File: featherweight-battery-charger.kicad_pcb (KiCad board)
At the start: 2 copper layers, 16 parts, among them J1 G125-MH104M4-04AD000P, J2 Conn_01x02, U1 MCP73832-2-OT, U2 TPS561208DDCR

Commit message: Started Layout and Routing
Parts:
- F1, R1: moved to B.Cu
- L1: value ASPI-4030S-4R7M-T (4.7uH) -> NRS4018T4R7MDGJ (4.7uH); footprint Inductor_SMD:L_Abracon_ASPI-4030S -> Inductor_SMD:L_Taiyo-Yuden_NR-40xx_HandSoldering
- moved J2 62.3 mm to (125.0, 119.6)
- moved U1 61.8 mm to (114.8, 121.3)
- moved C1 61.0 mm to (126.3, 116.3)
- moved R1 58.1 mm to (113.6, 120.3), turned to 180 degrees
- moved R2 55.9 mm to (111.8, 119.1), turned to -90 degrees
- moved D1 53.0 mm to (114.8, 118.3)
- moved L1 31.1 mm to (141.5, 67.7), turned to -90 degrees
- moved U2 27.7 mm to (146.6, 63.9), turned to 90 degrees
- moved R3 25.0 mm to (148.1, 59.8), turned to 90 degrees
- moved R4 24.0 mm to (147.2, 59.8), turned to -90 degrees
- moved C2 23.6 mm to (144.3, 63.2), turned to -90 degrees
- moved C3 20.3 mm to (146.6, 68.3), turned to 180 degrees
- moved C4 19.9 mm to (146.7, 69.2)
- moved C5 17.0 mm to (144.6, 68.3), turned to 180 degrees
- moved F1 12.8 mm to (149.5, 65.8), turned to 180 degrees
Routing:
- net GND: track 0.00 -> 5.30 mm
- net +12V: track 0.00 -> 4.77 mm
- net +5V: track 0.00 -> 3.24 mm
- net Net-(U2-VFB): track 0.00 -> 2.81 mm
- net Net-(U2-SW): track 13.8 -> 11.5 mm
- net /STAT: track 0.00 -> 2.25 mm
- net Net-(J1-+12V): track 0.00 -> 1.89 mm
- net Net-(D1-K): track 0.00 -> 1.75 mm

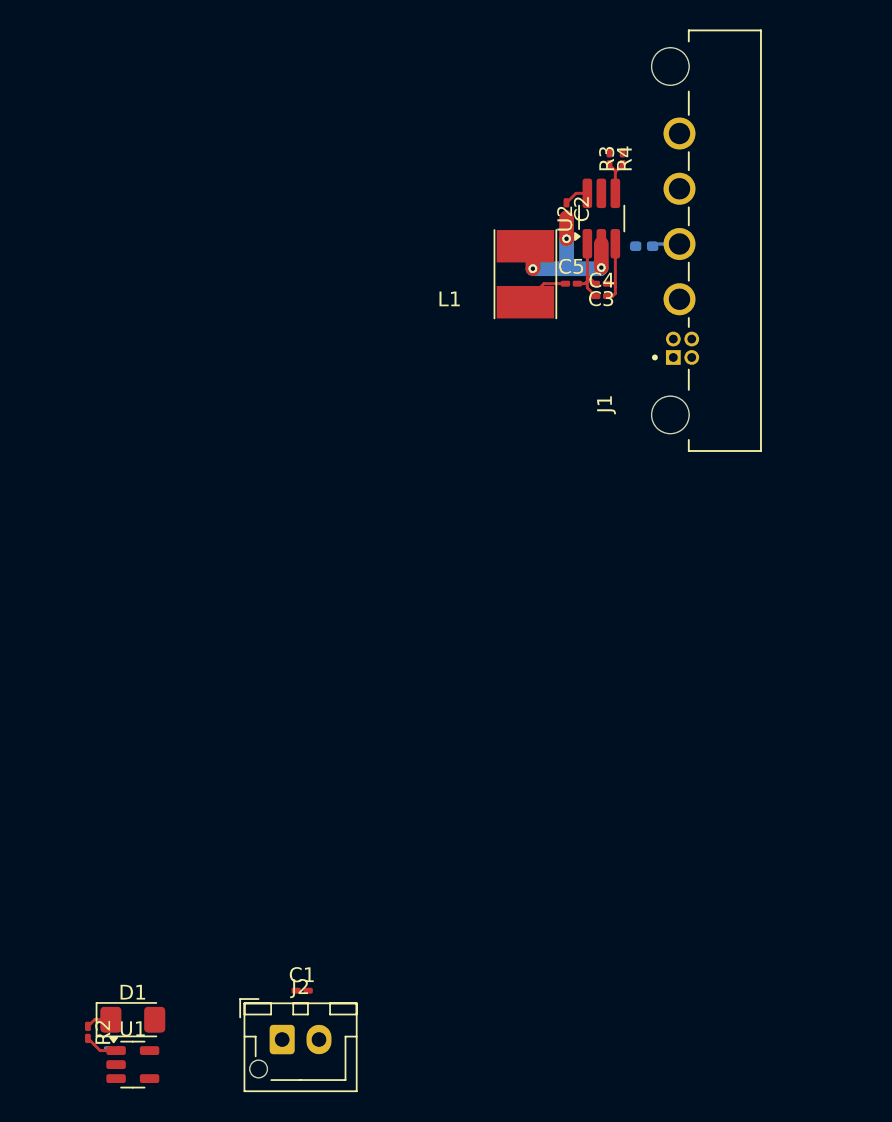
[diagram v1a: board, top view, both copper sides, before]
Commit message: Did most of the layout and routing, need to finish silkscreen and then check everything
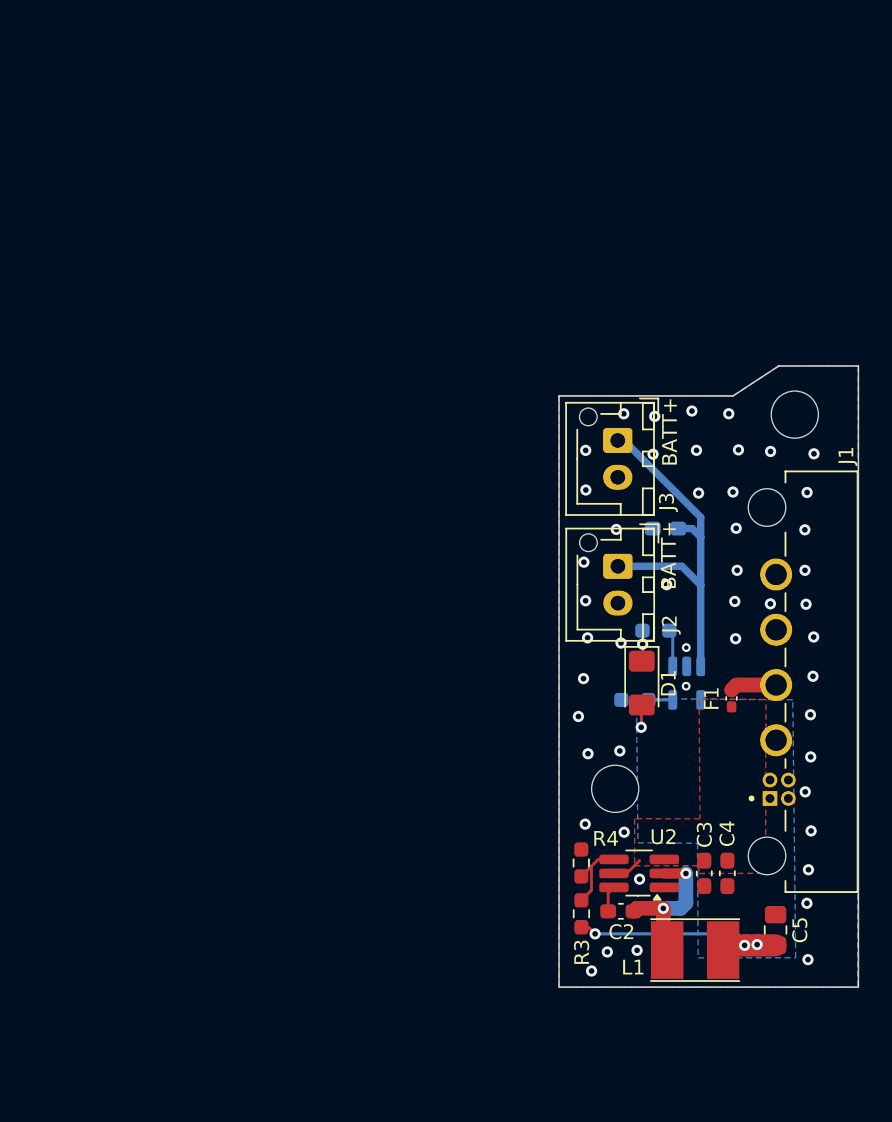
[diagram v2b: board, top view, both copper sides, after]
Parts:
- added H1: MountingHole, MountingHole:MountingHole_3.2mm_M3, F.Cu at (159.8, 77.2)
- added H2: MountingHole, MountingHole:MountingHole_3.2mm_M3, F.Cu at (147.6, 102.6)
- added J3: Conn_01x02, Connector_JST:JST_XH_B2B-XH-AM_1x02_P2.50mm_Vertical, F.Cu at (147.8, 79.0)
- C1: footprint Capacitor_SMD:C_0201_0603Metric_Pad0.64x0.40mm_HandSolder -> Capacitor_SMD:C_0603_1608Metric_Pad1.08x0.95mm_HandSolder; moved to B.Cu
- C2: footprint Capacitor_SMD:C_0201_0603Metric_Pad0.64x0.40mm_HandSolder -> Capacitor_SMD:C_0603_1608Metric_Pad1.08x0.95mm_HandSolder
- C3, C4: value 10uF -> CL10A106MA8NRNC (10uF); footprint Capacitor_SMD:C_0201_0603Metric_Pad0.64x0.40mm_HandSolder -> Capacitor_SMD:C_0603_1608Metric_Pad1.08x0.95mm_HandSolder
- C5: value 47uF -> GRM21BR61A476ME15L (47uF); footprint Capacitor_SMD:C_0201_0603Metric_Pad0.64x0.40mm_HandSolder -> Capacitor_SMD:C_0805_2012Metric_Pad1.18x1.45mm_HandSolder
- F1: moved to F.Cu
- R1, R3, R4: footprint Resistor_SMD:R_0201_0603Metric_Pad0.64x0.40mm_HandSolder -> Resistor_SMD:R_0603_1608Metric_Pad0.98x0.95mm_HandSolder
- R2: footprint Resistor_SMD:R_0201_0603Metric_Pad0.64x0.40mm_HandSolder -> Resistor_SMD:R_0603_1608Metric_Pad0.98x0.95mm_HandSolder; moved to B.Cu
- U1: moved to B.Cu
- moved R3 51.3 mm to (145.3, 111.1), turned to -90 degrees
- moved R4 47.8 mm to (145.3, 107.7)
- moved C2 47.8 mm to (148.0, 110.9), turned to 0 degrees
- moved L1 47.3 mm to (153.0, 113.6), turned to 0 degrees
- moved R2 47.2 mm to (150.3, 91.9), turned to 0 degrees
- moved C5 46.0 mm to (158.5, 112.2), turned to -90 degrees
- moved U1 45.7 mm to (152.4, 95.4), turned to -90 degrees
- moved U2 44.5 mm to (149.2, 108.4), turned to 180 degrees
- moved R1 42.5 mm to (148.9, 96.6)
- moved D1 41.4 mm to (149.4, 95.4), turned to -90 degrees
- moved C3 40.6 mm to (153.6, 108.4), turned to -90 degrees
- moved C4 40.1 mm to (155.2, 108.4), turned to 90 degrees
- moved C1 39.9 mm to (151.0, 85.0), turned to 180 degrees
- moved J2 39.4 mm to (147.8, 87.5), turned to -90 degrees
- moved F1 31.3 mm to (155.5, 96.5), turned to -90 degrees
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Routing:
- net Net-(J2-Pin_1): track 0.00 -> 25.8 mm
- net +5V: track 3.24 -> 16.3 mm, vias 0 -> 4
- net GND: track 5.30 -> 0.00 mm, vias 0 -> 49
- net +12V: track 4.77 -> 1.25 mm
- net Net-(U2-VFB): track 2.81 -> 5.28 mm
- net Net-(U2-SW): track 11.5 -> 9.84 mm, vias 3 -> 2
- net Net-(U1-PROG): track 0.00 -> 1.46 mm
- net Net-(J1-+12V): track 1.89 -> 3.17 mm
- net Net-(D1-K): track 1.75 -> 2.03 mm, vias 0 -> 1
- added copper zone on F.Cu, net +12V
- added copper zone on B.Cu, net +5V
- added copper zone on B.Cu, net GND
- added copper zone on F.Cu, net GND
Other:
- board outline added: 20.3 x 42.2 mm
- board text added: "BATT+"

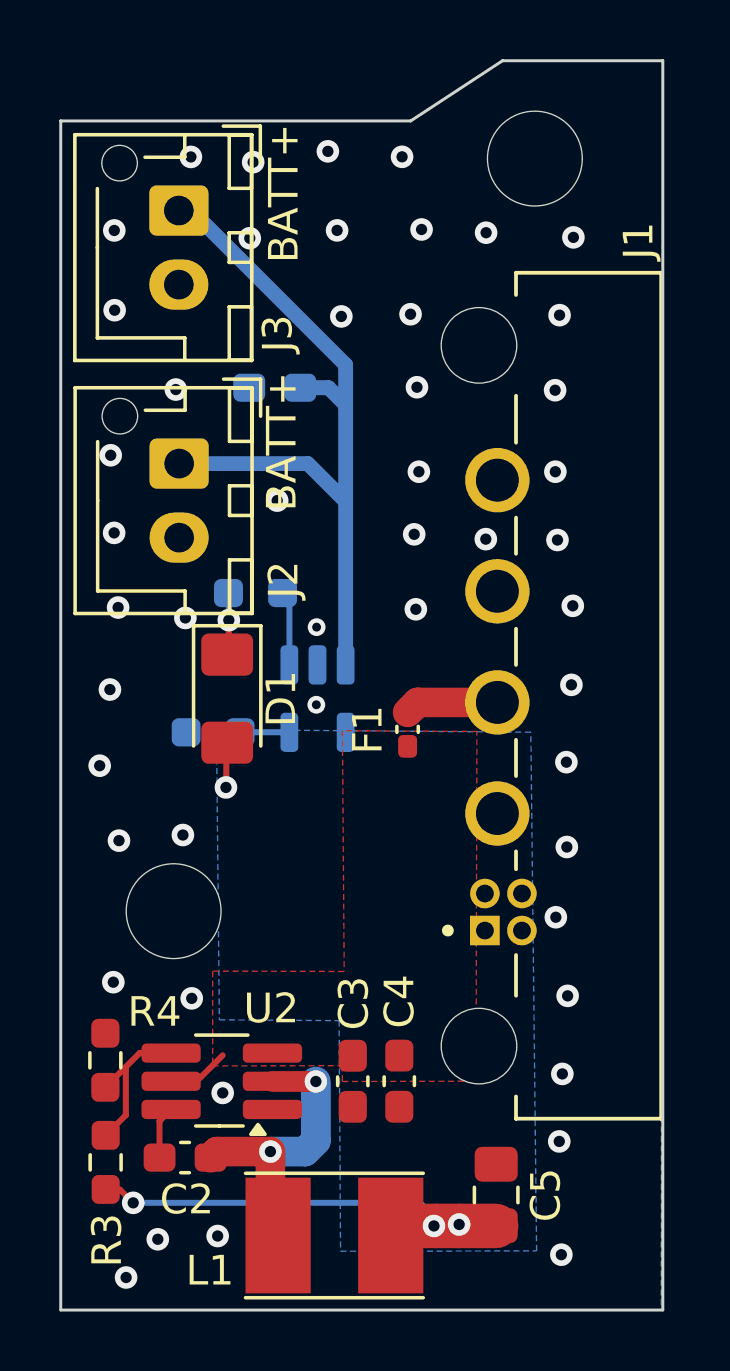
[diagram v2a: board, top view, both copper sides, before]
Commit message: Fixed some routing and silkscreen, should be done hopefully
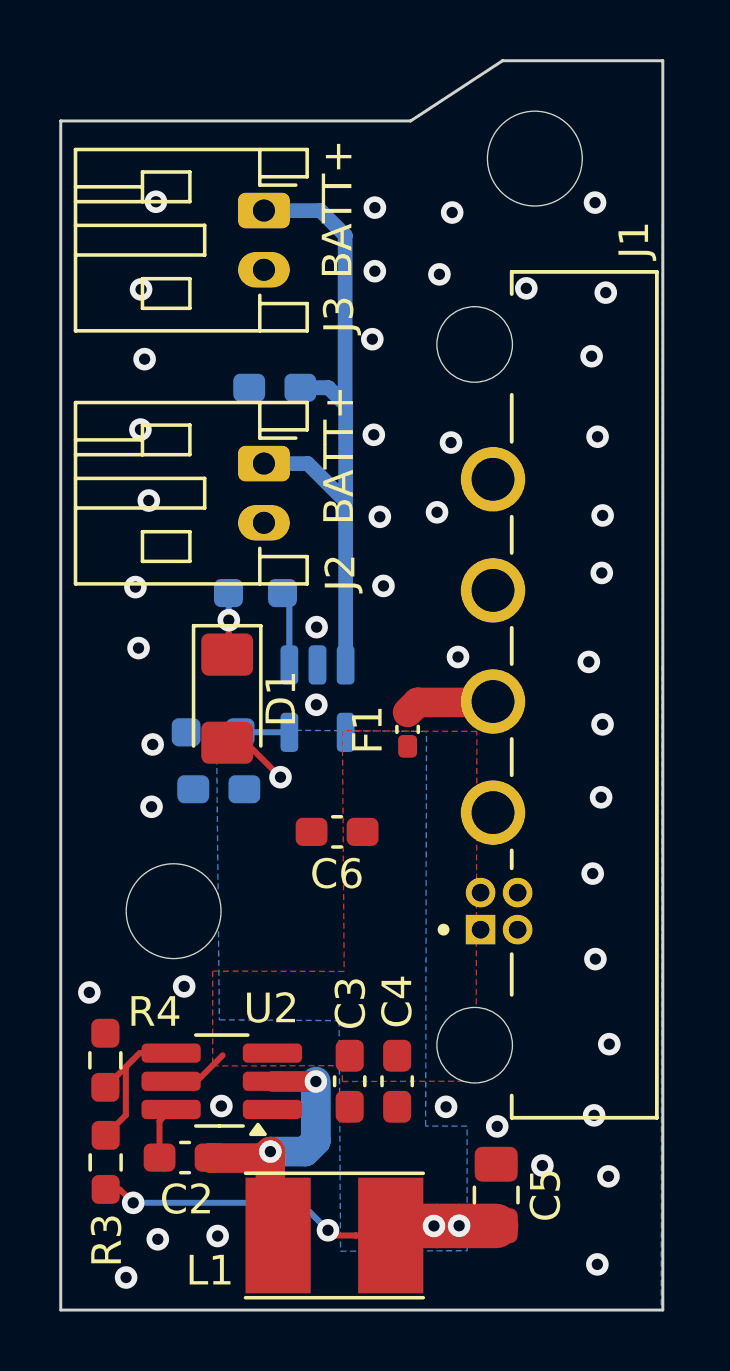
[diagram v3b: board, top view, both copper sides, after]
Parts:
- added C6: 0.1uF, Capacitor_SMD:C_0603_1608Metric_Pad1.08x0.95mm_HandSolder, F.Cu at (153.1, 99.9)
- added C7: 0.1uF, Capacitor_SMD:C_0603_1608Metric_Pad1.08x0.95mm_HandSolder, B.Cu at (149.1, 98.5)
- F1: value ERB-RD0R50X -> ERB-RD0R50X (500mA)
- J2, J3: footprint Connector_JST:JST_XH_B2B-XH-AM_1x02_P2.50mm_Vertical -> Connector_JST:JST_PH_S2B-PH-K_1x02_P2.00mm_Horizontal
- moved J3 2.87 mm to (150.6, 79.0)
- moved J2 2.86 mm to (150.6, 87.5)
- moved J1 0.15 mm to (161.4, 95.3)
- moved C3 0.10 mm to (153.5, 108.4)
- moved C4 0.07 mm to (155.1, 108.4)
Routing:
- net Net-(J2-Pin_1): track 25.8 -> 22.7 mm
- net +5V: track 16.3 -> 15.1 mm, vias 4 -> 5
- net GND: vias 49 -> 47

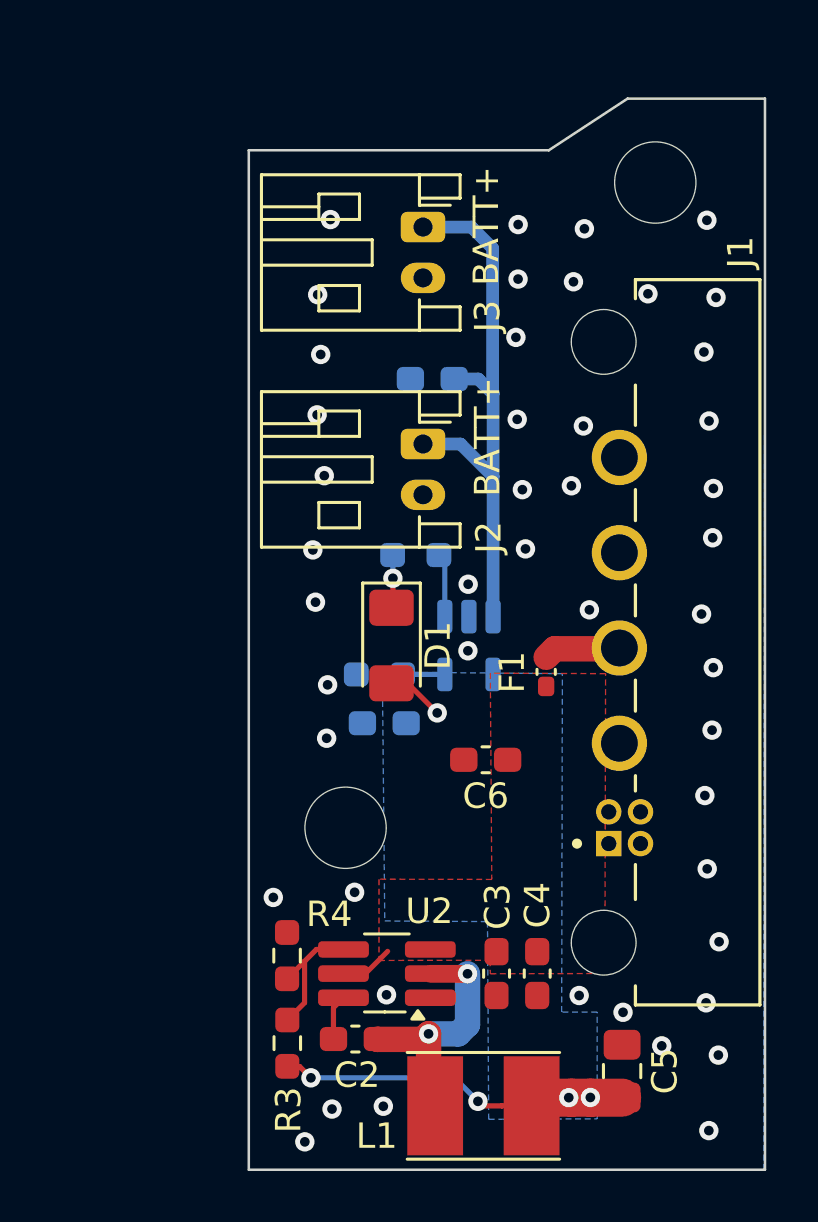
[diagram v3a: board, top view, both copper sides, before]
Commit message: Changed Layout and Routing
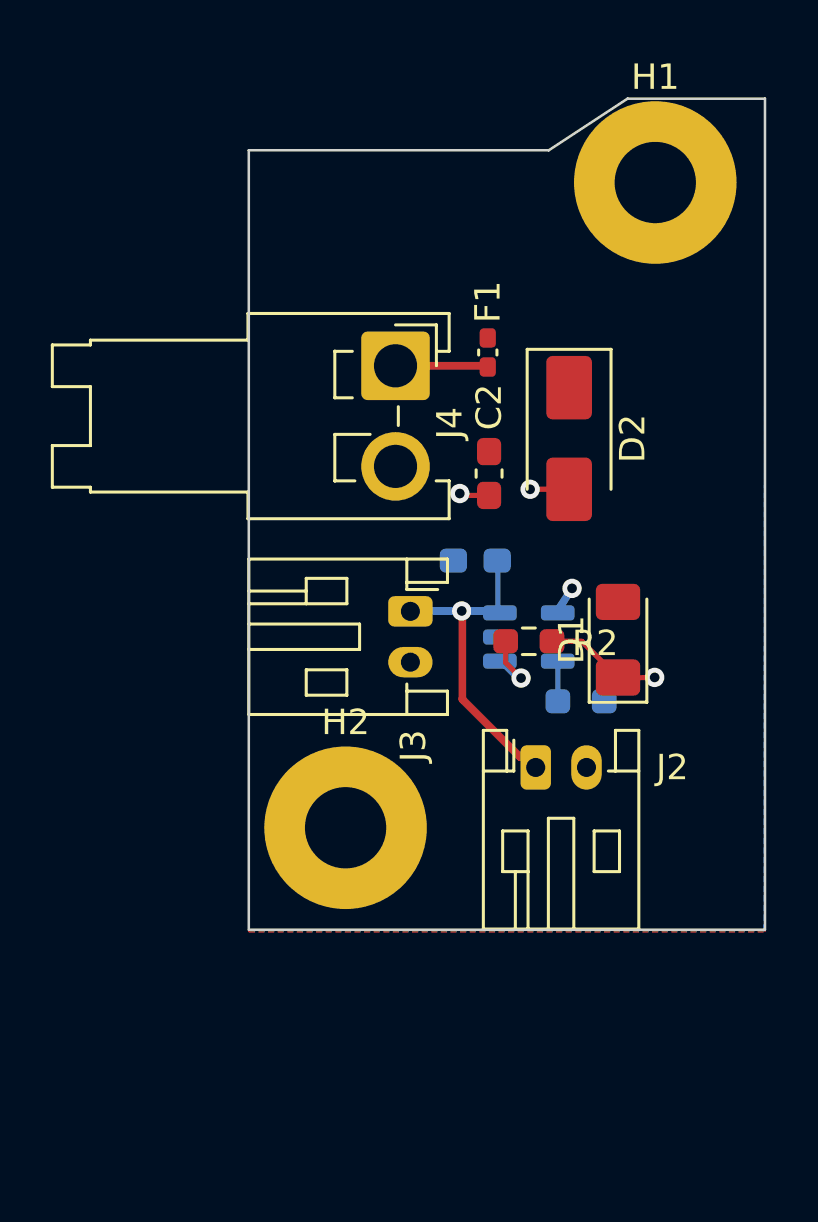
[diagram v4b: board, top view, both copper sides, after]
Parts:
- removed C1: 4.7uF, Capacitor_SMD:C_0603_1608Metric_Pad1.08x0.95mm_HandSolder
- removed C4: CL10A106MA8NRNC (10uF), Capacitor_SMD:C_0603_1608Metric_Pad1.08x0.95mm_HandSolder
- removed C5: GRM21BR61A476ME15L (47uF), Capacitor_SMD:C_0805_2012Metric_Pad1.18x1.45mm_HandSolder
- removed C6, C7: 0.1uF, Capacitor_SMD:C_0603_1608Metric_Pad1.08x0.95mm_HandSolder
- removed J1: G125-MH104M4-04AD000P, canhw:connector_Harwin_G125-MH104M4-04AD000P
- removed L1: NRS4018T4R7MDGJ (4.7uH), Inductor_SMD:L_Taiyo-Yuden_NR-40xx_HandSoldering
- removed R3: 54.9k, Resistor_SMD:R_0603_1608Metric_Pad0.98x0.95mm_HandSolder
- removed R4: 10k, Resistor_SMD:R_0603_1608Metric_Pad0.98x0.95mm_HandSolder
- removed U2: TPS561208DDCR, Package_TO_SOT_SMD:TSOT-23-6_HandSoldering
- added D2: SMAJ5.0A, Diode_SMD:D_SMA, F.Cu at (156.4, 87.3)
- added J4: Conn_01x02, Connector_JST:JST_VH_S2P-VH_1x02_P3.96mm_Horizontal, F.Cu at (149.5, 84.4)
- C2: value 100nF -> 1uF
- C3: value CL10A106MA8NRNC (10uF) -> 4.7uF; moved to B.Cu
- H1, H2: footprint MountingHole:MountingHole_3.2mm_M3 -> MountingHole:MountingHole_3.2mm_M3_Pad
- R2: moved to F.Cu
- moved C2 22.9 mm to (153.2, 88.7), turned to -90 degrees
- moved C3 16.3 mm to (152.7, 92.1), turned to 180 degrees
- moved J3 15.1 mm to (150.1, 94.1)
- moved J2 13.5 mm to (155.1, 100.2), turned to 0 degrees
- moved F1 12.8 mm to (153.2, 83.9), turned to 90 degrees
- moved D1 8.92 mm to (158.3, 95.2), turned to 90 degrees
- moved R1 8.01 mm to (156.8, 97.6), turned to 0 degrees
- moved R2 5.60 mm to (154.8, 95.3), turned to 180 degrees
- moved U1 2.38 mm to (154.8, 95.1), turned to 0 degrees
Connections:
- C2 pad 1: Net-(U2-VBST) -> +5V
- C2 pad 2: Net-(U2-SW) -> GND
- C3 pad 1: +12V -> Net-(J2-Pin_1)
- F1 pad 2: +12V -> +5V
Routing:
- net +5V: track 15.1 -> 1.13 mm, vias 5 -> 1
- net Net-(J2-Pin_1): track 22.7 -> 12.5 mm, vias 0 -> 1
- net Net-(U2-SW): track 9.84 -> 0.00 mm, vias 2 -> 0
- net Net-(U2-VFB): track 5.28 -> 0.00 mm
- net GND: track 0.00 -> 2.91 mm, vias 47 -> 2
- net Net-(D1-K): track 2.01 -> 4.64 mm
- net Net-(U2-VBST): track 1.70 -> 0.00 mm
- net +12V: track 1.25 -> 0.00 mm
- net /STAT: track 2.20 -> 2.81 mm, vias 0 -> 1
- net Net-(J4-Pin_1): track 3.17 -> 3.71 mm
- added copper zone on F.Cu, net +5V
- removed copper zone on F.Cu, net +12V
- removed copper zone on B.Cu, net +5V
- removed copper zone on F.Cu, net GND
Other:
- board size 20.3 x 42.2 mm -> 20.3 x 32.7 mm
- board text removed: "BATT+"
